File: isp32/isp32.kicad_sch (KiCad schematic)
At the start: 97 parts, among them J1 BAT1, J10 LoRa_ANT, J12 Micro_SD_Card, J2 Switching, J3 USB_C_Receptacle_USB2.0, J4 ESP_JTAG, J5 GPS_ANT, J6 F0, J7 F1, J9 ANT, M1 Motor_Servo, M2 Motor_Servo, M3 Motor_Servo, M4 Motor_Servo, Q1 BSS138, Q2 BSS138, Q3 IRLML6402, Q4 BSS138, Q5 IRLML6402, Q6 S8050, SW1 RST, SW2 IO0, U10 BMP280, U11 MPU-9250, U2 USBLC6-2SC6, U3 STM32F030F4Px, U4 AMS1117-3.3, U5 MP2303ADN, U6 24LC32, U7 NEO-XM, U8 ESP32-S3-WROOM-1U, U9 RFM98W-315S2

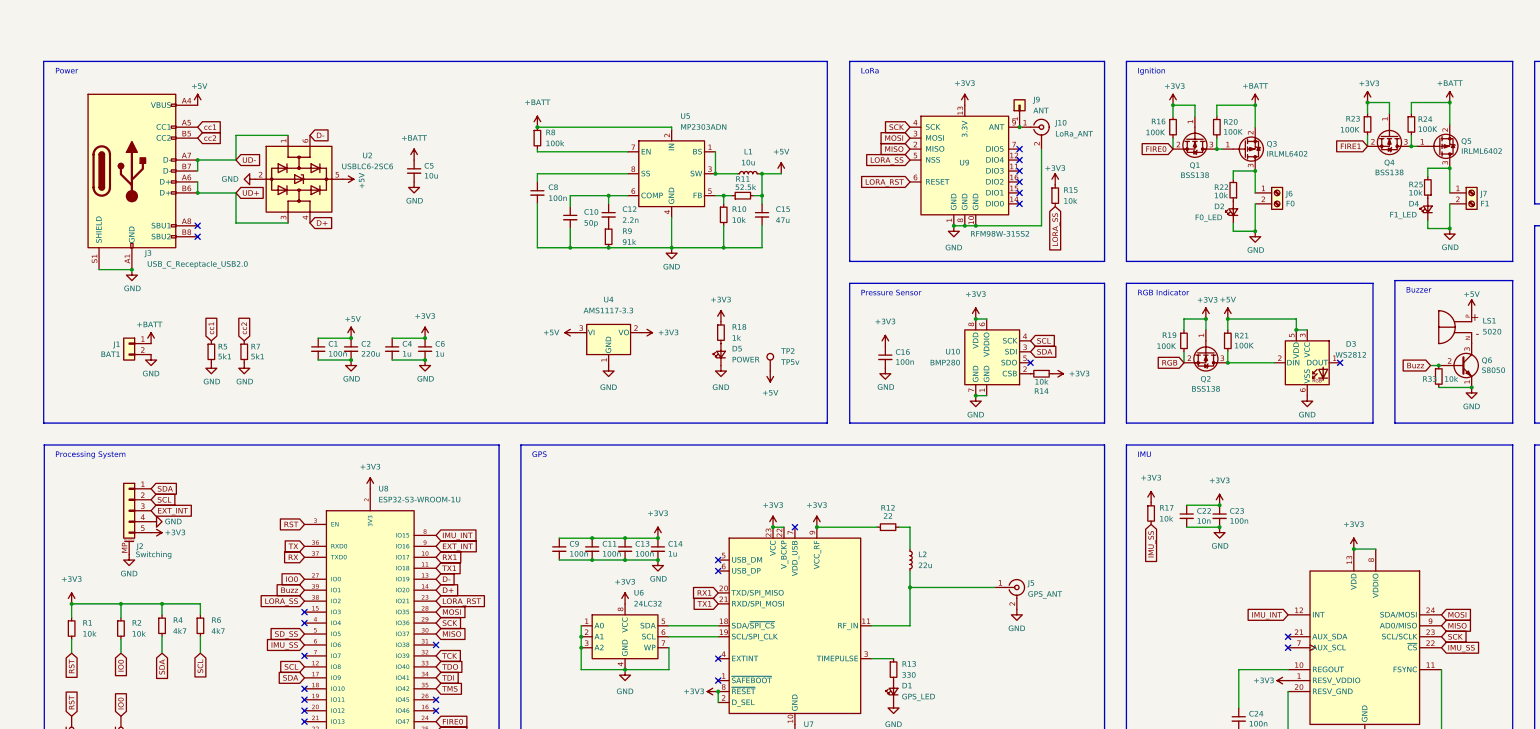
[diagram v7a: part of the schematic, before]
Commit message: Change power circuits
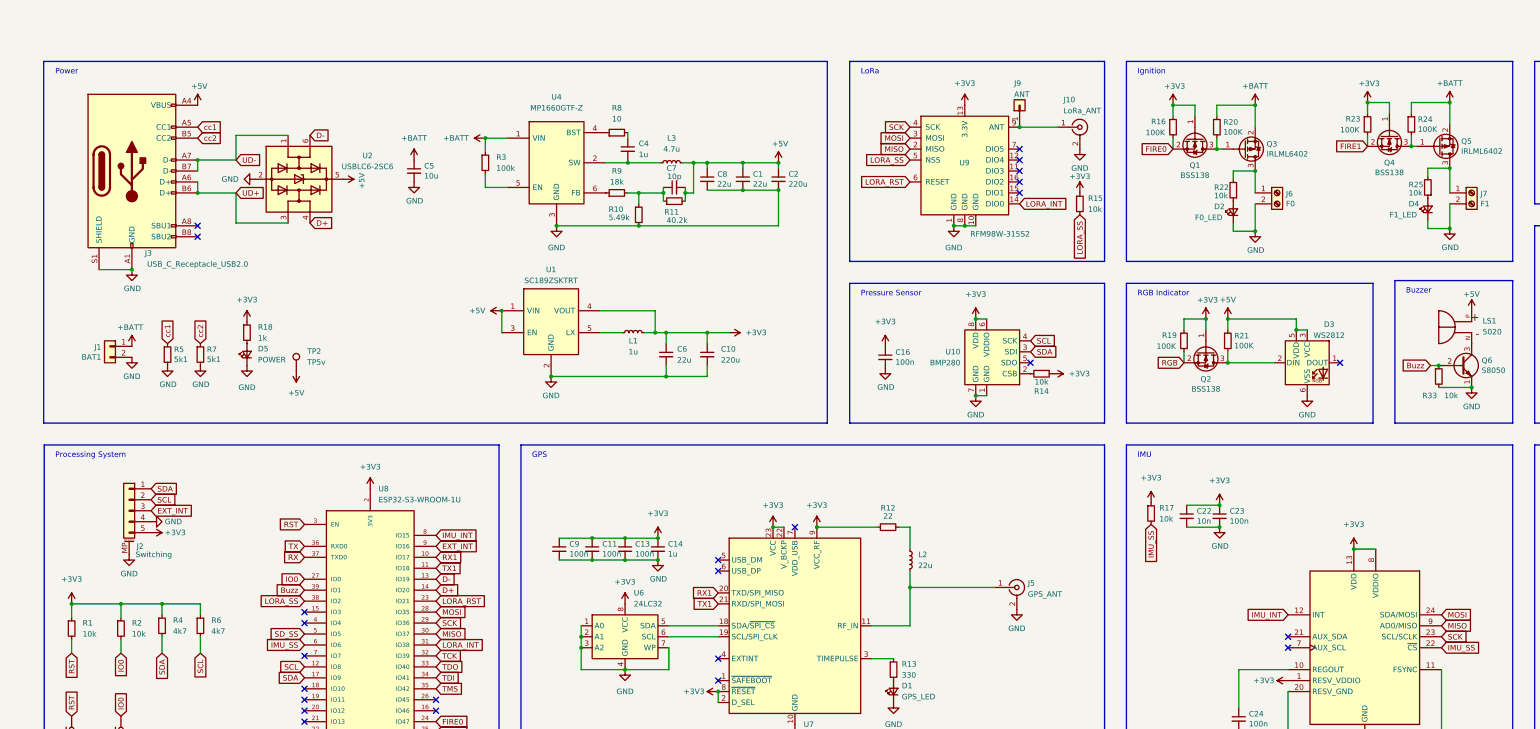
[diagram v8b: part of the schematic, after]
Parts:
- removed C12: 2.2n, Capacitor_SMD:C_0603_1608Metric, symbol Device:C_Small
- removed C15: 47u, Capacitor_SMD:C_0603_1608Metric, symbol Device:C_Small
- removed U4: AMS1117-3.3, Package_TO_SOT_SMD:SOT-223-3_TabPin2, symbol Regulator_Linear:AMS1117-3.3
- removed U5: MP2303ADN, Package_SO:SOIC-8-1EP_3.9x4.9mm_P1.27mm_EP2.62x3.51mm, symbol Regulator_Switching:MP2303ADN
- added C7: 10p, Capacitor_SMD:C_0603_1608Metric, symbol Device:C_Small
- added L3: 4.7u, Inductor_SMD:L_Sunlord_SWPA5020S, symbol Device:L_Small
- added R3: 100k, Resistor_SMD:R_0603_1608Metric, symbol Device:R_Small
- added U1: SC189ZSKTRT, Package_TO_SOT_SMD:SOT-23-5, symbol SC189ZSKTRT:SC189ZSKTRT
- added U4: MP1660GTF-Z, Package_TO_SOT_SMD:SOT-563, symbol MP1660GTF-Z:MP1660GTF-Z
- C1, C8: value 100n -> 22u
- C10: value 50p -> 220u; footprint Capacitor_SMD:C_0603_1608Metric -> Capacitor_Tantalum_SMD:CP_EIA-3528-12_Kemet-T
- C6: value 1u -> 22u; footprint Capacitor_SMD:C_0603_1608Metric -> Capacitor_SMD:C_0805_2012Metric
- L1: value 10u -> 1u; footprint Inductor_SMD:L_Abracon_ASPI-0630LR -> Inductor_SMD:L_Bourns-SRN4018
- R10: value 10k -> 5.49k
- R11: value 52.5k -> 40.2k
- R8: value 100k -> 10
- R9: value 91k -> 18k
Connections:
- net +3V3: now also C10.1, L1.2, U1.4 (VOUT); no longer C4.1
- net +5V: now also C8.1, C7.2, L3.2, U1.1 (VIN), U1.3 (EN); no longer L1.2
- net +BATT: now also R3.1, U4.1 (VIN); no longer R8.1
- net GND: now also U1.2 (GND), U4.3 (GND); no longer C4.2, R9.2
- net LORA_INT: now reaches U9.14 (DIO0)
- net LORA_INT: now also U8.31 (IO38)
- net at R9.1: now also U4.6 (FB)
- net at L1.1: now also U1.5 (LX)
- net at R8.2: now also C4.1
- net at R10.1, R11.1: now also R9.2, C7.1
- new net: R3.2, U4.5 (EN)
- new net: C4.2, L3.1, U4.2 (SW)
- new net: R8.1, U4.4 (BST)
- no-connect marks 38 -> 36
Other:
- moved on the sheet: C1, C2, D5, J1, J10, R15, R18, R5, R7, TP2
